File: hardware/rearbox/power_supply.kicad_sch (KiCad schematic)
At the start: 36 parts, among them U3 LM62440-Q1, U4 TLV743P

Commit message: Changed power section
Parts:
- removed C19: 22u, Capacitor_SMD:C_0603_1608Metric, symbol Device:C_Small
- removed F2: 350mA, Local_Library:Fuse_1812_4532Metric, symbol Device:Polyfuse_Small
- removed L3: 1u5, Local_Library:L_Abracon_ASPI-4030S, symbol Device:L
- removed R4: 100k, Resistor_SMD:R_0603_1608Metric, symbol Device:R_Small
- removed R5: 24k9, Resistor_SMD:R_0603_1608Metric, symbol Device:R_Small
- removed R6: 1k, Resistor_SMD:R_0603_1608Metric, symbol Device:R_Small
- removed TP5, TP6: TestPoint_Small, TestPoint:TestPoint_Pad_D1.0mm, symbol Connector:TestPoint_Small
- removed U3: LM62440-Q1, Local_Library:IC_LM61460AANRJRR, symbol LM62440:LM62440
- added F5: 1.5A, Fuse:Fuse_1812_4532Metric, symbol Device:Polyfuse_Small
- added IC2: TPS54202HDDCR, Package_TO_SOT_SMD:SOT-23-6, symbol SamacsysNew:TPS54202HDDCR
- added L3: 68uH/1.4A, Inductor_SMD:L_TDK_VLS6045EX_VLS6045AF, symbol Samacsys_kicad_sym:SRR4028-271Y
- added R135: 510k, Resistor_SMD:R_0603_1608Metric, symbol Device:R_Small
- added R136: 43k, Resistor_SMD:R_0603_1608Metric, symbol Device:R_Small
- added R137: 13.3k, Resistor_SMD:R_0603_1608Metric, symbol Device:R_Small
- added R138: 100k, Resistor_SMD:R_0603_1608Metric, symbol Device:R_Small
- C14: value 220n -> 22uF; Manufacturer_Name (none) -> MCASH21GCC7684MTCA1J; Manufacturer_Part_Number (none) -> CL21A107MQYNNWE; Mouser Part Number (none) -> 810-C2012X5R1V226MAC; Rated Voltage 35V -> (none)
- C15: value 1u -> 22uF; footprint Capacitor_SMD:C_0603_1608Metric -> Capacitor_SMD:C_0805_2012Metric; Manufacturer_Name (none) -> MCASH21GCC7684MTCA1J; Manufacturer_Part_Number (none) -> CL21A107MQYNNWE; Mouser Part Number (none) -> 810-C2012X5R1V226MAC
- C16: value 220n -> 100nF; footprint Capacitor_SMD:C_0805_2012Metric -> Capacitor_SMD:C_0603_1608Metric; Manufacturer_Name (none) -> --; Manufacturer_Part_Number (none) -> C0603C104J3RACTU; Mouser Part Number (none) -> --; Mouser Price/Stock (none) -> https://www.mouser.pl/ProductDetail/KEMET/C0603C104J3RACTU?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; Rated Voltage 35V -> (none)
- C17: value 100n -> 100nF; Manufacturer_Name (none) -> --; Manufacturer_Part_Number (none) -> C0603C104J3RACTU; Mouser Part Number (none) -> --; Mouser Price/Stock (none) -> https://www.mouser.pl/ProductDetail/KEMET/C0603C104J3RACTU?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
- C18: value 22p -> 22uF; footprint Capacitor_SMD:C_0603_1608Metric -> Capacitor_SMD:C_0805_2012Metric; Manufacturer_Name (none) -> MCASH21GCC7684MTCA1J; Manufacturer_Part_Number (none) -> CL21A107MQYNNWE; Mouser Part Number (none) -> 810-C2012X5R1V226MAC
- C20: value 22u -> 22uF; footprint Capacitor_SMD:C_0603_1608Metric -> Capacitor_SMD:C_0805_2012Metric; Manufacturer_Name (none) -> MCASH21GCC7684MTCA1J; Manufacturer_Part_Number (none) -> CL21A107MQYNNWE; Mouser Part Number (none) -> 810-C2012X5R1V226MAC
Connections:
- net +5V_FUSED is gone; now on net +5V: C21.1, TP7.1, U4.1 (IN), U4.3 (EN)
- net FB is gone; now on net GND: C18.2
- net +5V: now also F5.2; no longer C20.1
- net GND: now also C14.1, C15.1, C16.1, IC2.1 (GND), R136.2, R137.1; no longer C14.2, C15.2, C16.2
- net SW_5V: now reaches C17.2
- net SW_5V: now also IC2.2 (SW), L3.1
- net 5V_UNFUSED: now reaches C18.1
- net 5V_UNFUSED: now also C20.1, F5.1, L3.2, R138.2
- net SW renamed BOOT_5V
- net BOOT_5V: now also IC2.6 (BOOT)
- net VIN: no longer names the net of C12.1, C13.1, L2.2, TP4.1
- net VIN: now also C14.2, C15.2, C16.2, IC2.3 (VIN), R135.2; no longer C14.1, C16.1
- new net EN_5V: IC2.5 (EN), R135.1, R136.1
- new net FB_5V: IC2.4 (FB), R137.2, R138.1
- no-connect marks 1 -> 0
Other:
- note removed: "V_{out} = 5 V"
- moved on the sheet: C10, C11, C12, C13, C22, C23, F1, F3, F4, L2, L4, TP10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

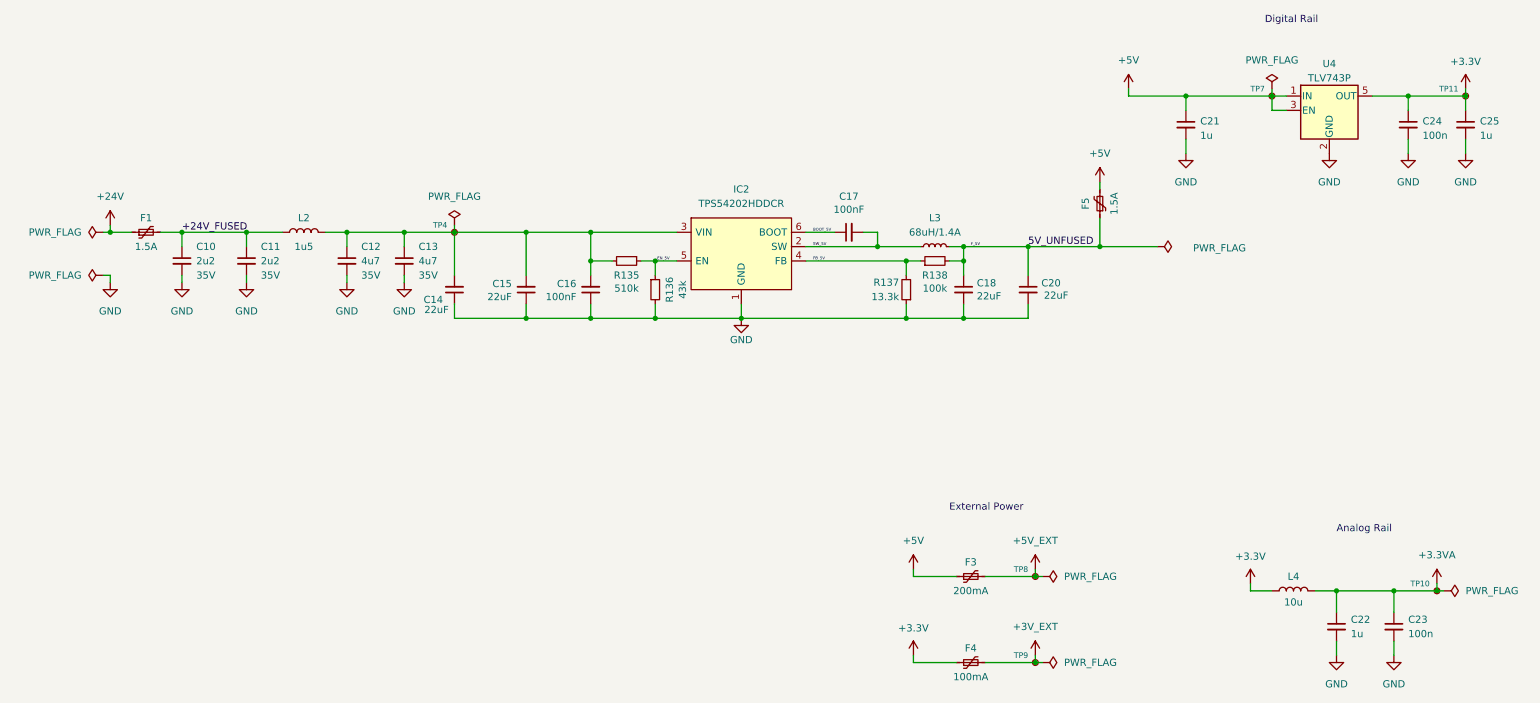
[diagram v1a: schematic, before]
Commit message: Added ESD protection to power section
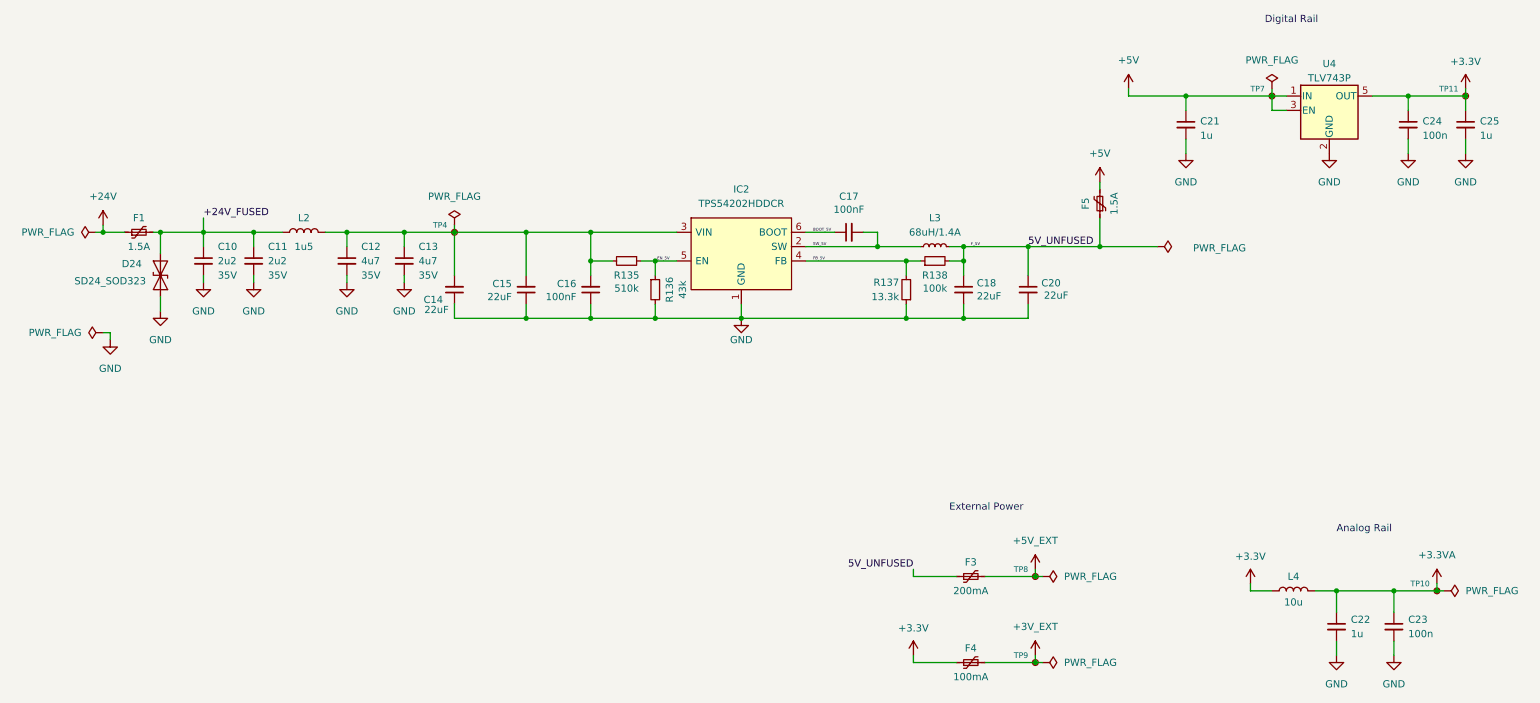
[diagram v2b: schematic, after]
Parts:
- added D24: SD24_SOD323, Diode_SMD:D_SOD-323, symbol Diode:SD24_SOD323
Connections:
- net +24V_FUSED: now also D24.2 (A2)
- net +5V: no longer F3.1
- net 5V_UNFUSED: now also F3.1
- net GND: now also D24.1 (A1)
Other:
- moved on the sheet: C10, C11, F1

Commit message: Sync :(
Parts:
- C15, C18, C20: value 22uF -> 22u
- C16, C17: value 100nF -> 100n
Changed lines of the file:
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@@
 			)
 		)
-		(property "Value" "22uF"
+		(property "Value" "22u"
 			(at 193.294 82.296 0)
 			(effects
@@
 			)
 		)
-		(property "Value" "22uF"
+		(property "Value" "22u"
 			(at 99.06 82.55 0)
 			(effects
@@
 			)
 		)
-		(property "Value" "100nF"
+		(property "Value" "100n"
 			(at 158.75 67.0814 90)
 			(effects
@@
 			)
 		)
-		(property "Value" "22uF"
+		(property "Value" "22u"
 			(at 181.4068 82.423 0)
 			(effects
@@
 			)
 		)
-		(property "Value" "100nF"
+		(property "Value" "100n"
 			(at 110.49 82.55 0)
 			(effects
